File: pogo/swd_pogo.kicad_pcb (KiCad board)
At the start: 2 copper layers, 46.8 x 28.2 mm, 16 parts, among them J1 CONN_02X05, J2 Conn_02x04_Odd_Even, J3 CONN_01X04, J4 CONN_01X04

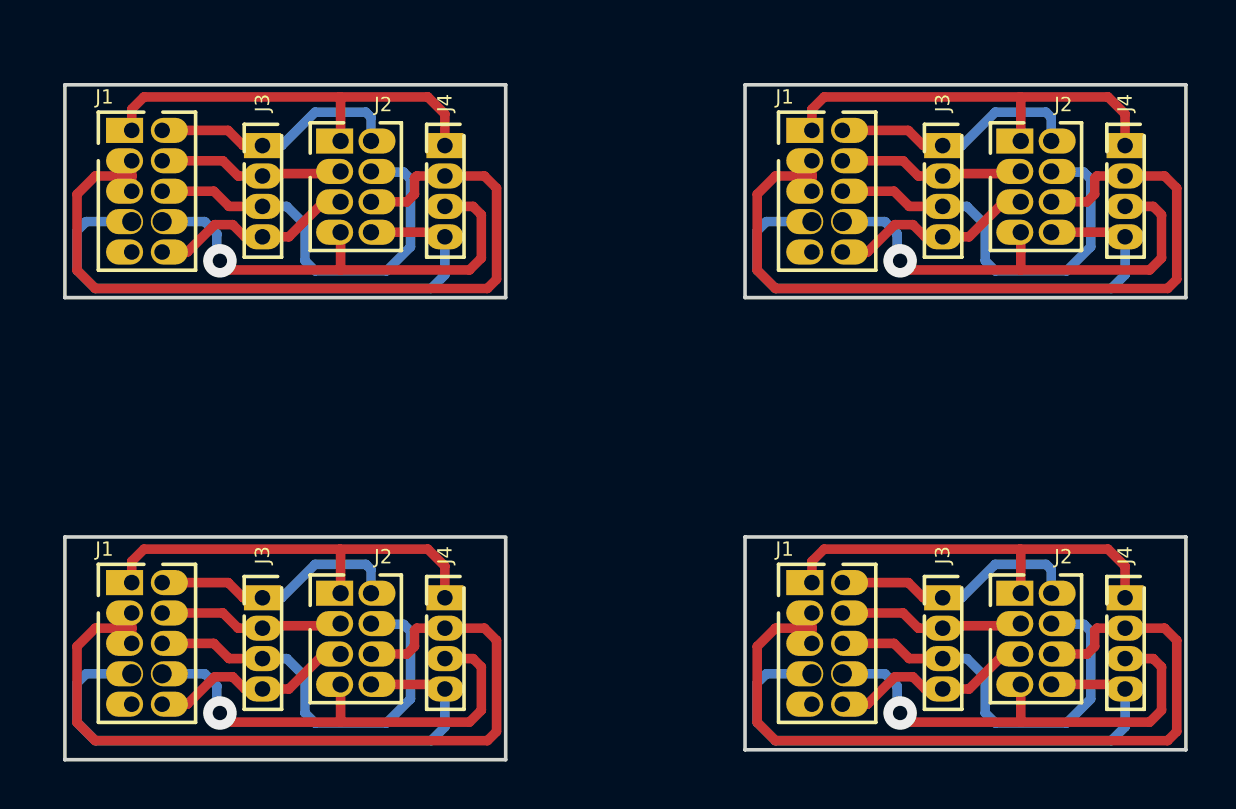
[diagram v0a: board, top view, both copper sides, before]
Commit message: Too many untracked changes: LCD boards update and switch to KiCAD version 5
Update the Nokia LCD breakout boards
Add more KiCAD simulation projects
Update most projects to KiCAD version 5
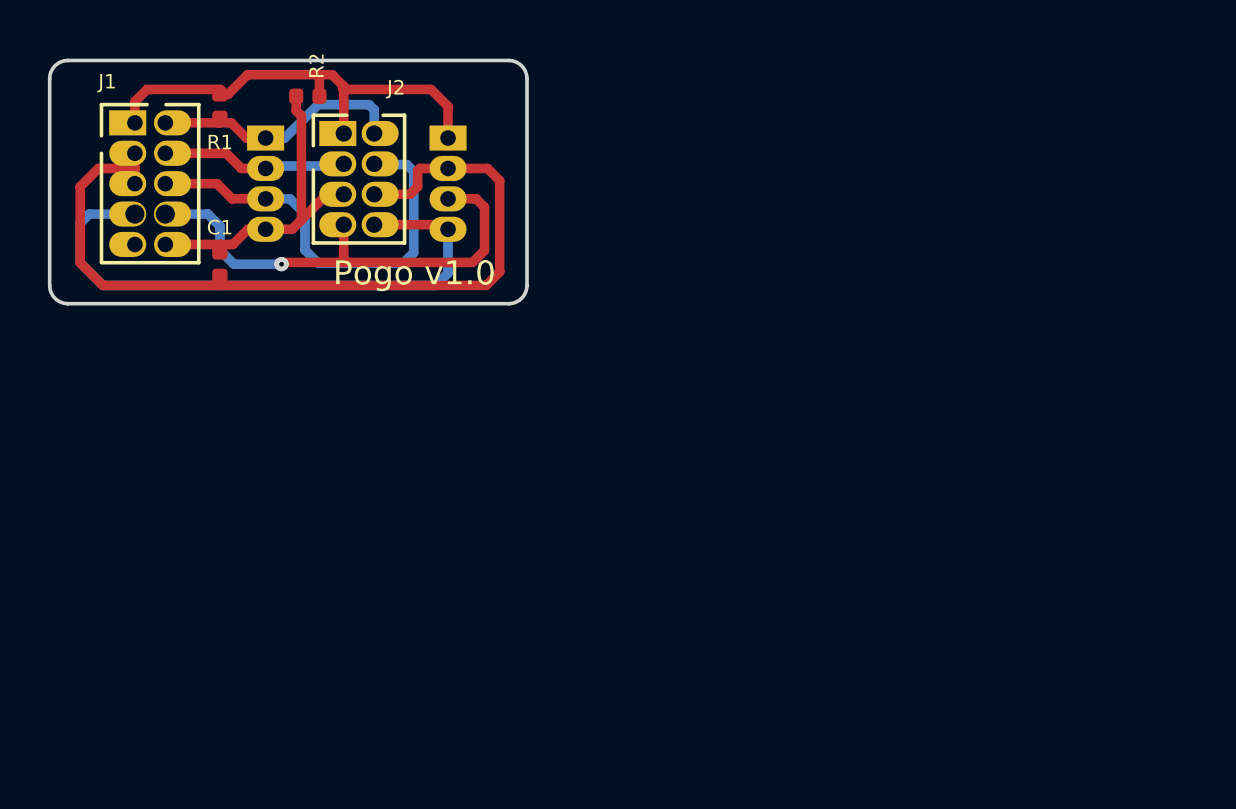
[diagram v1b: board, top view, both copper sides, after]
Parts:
- removed the J1 at (50.4, 99.3)
- removed the J1 at (78.8, 99.3)
- removed the J1 at (78.8, 80.4)
- removed the J2 at (59.1, 99.7)
- removed the J2 at (87.6, 99.7)
- removed the J2 at (87.6, 80.8)
- removed the J3 at (55.9, 99.9)
- removed the J3 at (84.3, 99.9)
- removed the J3 at (84.3, 81.0)
- removed the J4 at (63.5, 99.9)
- removed the J4 at (91.9, 99.9)
- removed the J4 at (91.9, 81.0)
- added C1: 100nF, Capacitor_SMD:C_0402_1005Metric, F.Cu at (54.1, 86.0)
- added R1: 10K, Resistor_SMD:R_0402_1005Metric, F.Cu at (54.1, 79.4)
- added R2: 10K, Resistor_SMD:R_0402_1005Metric, F.Cu at (57.8, 79.0)
- J3, J4: moved to B.Cu
- moved J1 0.34 mm to (50.6, 80.1)
- moved J4 0.34 mm to (63.6, 80.7)
- moved J2 0.34 mm to (59.3, 80.5)
- moved J3 0.34 mm to (56.0, 80.7)
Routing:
- net GND: track 140.6 -> 35.7 mm
- net UARTTX: track 99.1 -> 25.1 mm
- net UARTRX: track 80.1 -> 20.1 mm, vias 4 -> 1
- net SWDTRACE: track 70.6 -> 18.0 mm
- net 3v3: track 70.6 -> 19.5 mm
- net SWDIO: track 42.6 -> 10.9 mm
- net SWDCLK: track 31.2 -> 7.80 mm
- net RESET: track 35.0 -> 14.1 mm
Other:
- board size 46.8 x 28.2 mm -> 19.9 x 10.2 mm
- rule via_min_drill: 0.3 -> 0.2
- board text added: "31-08-2020"
- board text added: "Karibe (K) Ltd"
- board text added: "Pogo v1.0"
